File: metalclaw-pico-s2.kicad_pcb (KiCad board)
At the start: 2 copper layers, 21 x 51 mm, 73 parts, among them J1 USB_C_Receptacle_USB2.0_14P, J2 Conn_01x05, J3 Conn_02x05_Odd_Even, J4 Conn_Coaxial, SW1 SW_Push, SW2 SW_Push, U1 ESP32-S2, U2 MX25L3236FM2I-08G-TR, U3 APS6404L-3SQRx-SN, U5 XC6220B331MR, Y1 XRCGB40M000F1S2FR0

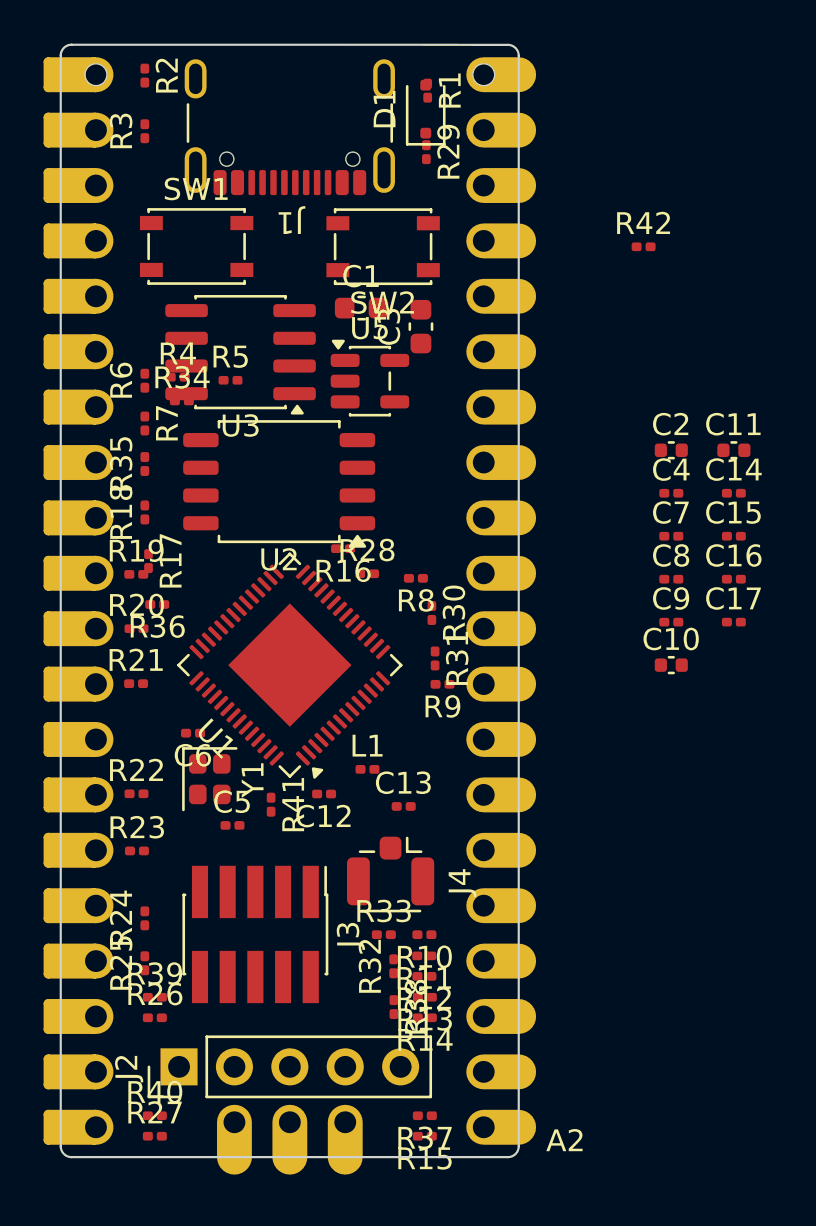
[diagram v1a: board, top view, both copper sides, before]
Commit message: Specify more passive component parts
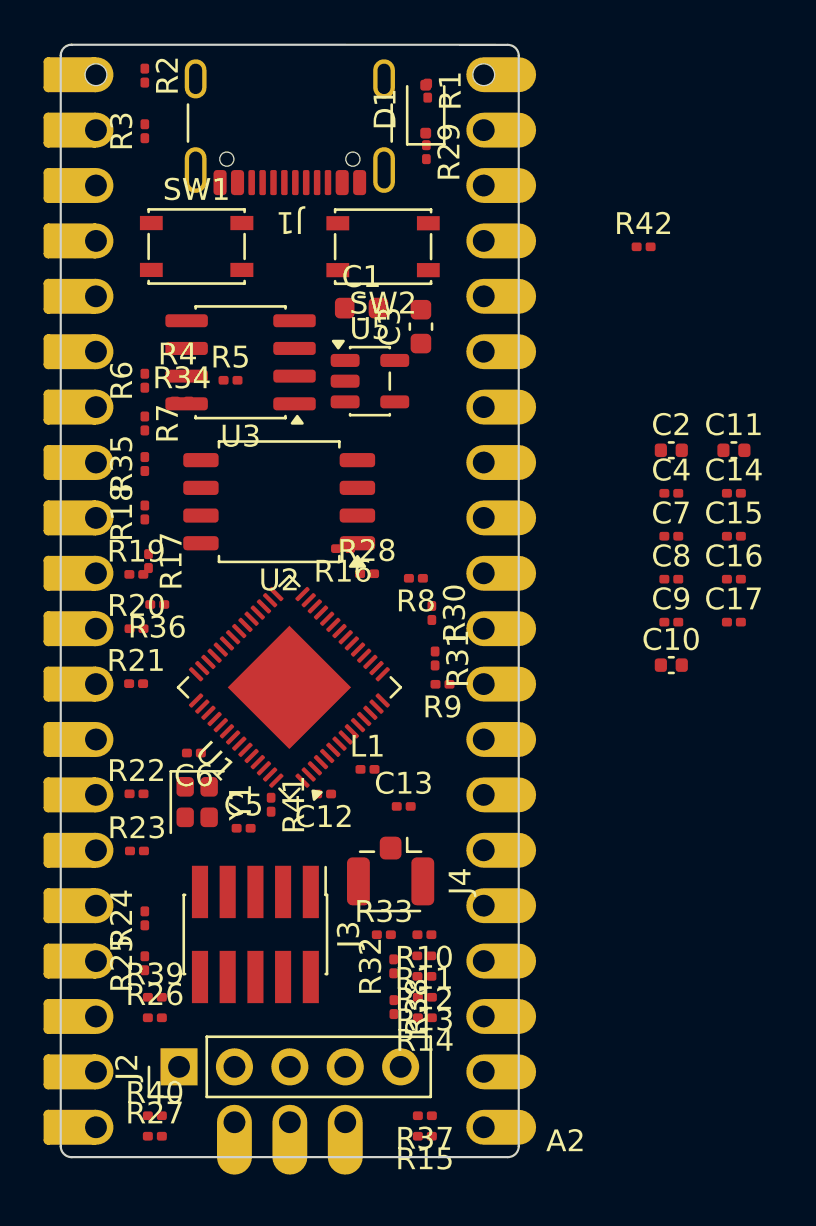
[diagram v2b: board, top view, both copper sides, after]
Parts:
- moved Y1 1.20 mm to (159.6, 108.1)
- moved U1 1.02 mm to (163.8, 102.8)
- moved U2 0.92 mm to (163.3, 94.3)
- moved C6 0.91 mm to (159.4, 105.8)
- moved C5 0.53 mm to (161.7, 109.3)
- moved U3 0.47 mm to (161.6, 87.9)
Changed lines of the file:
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@@
 	(footprint "Capacitor_SMD:C_0201_0603Metric"
 		(layer "F.Cu")
-		(at 161.18 109.16)
+		(at 161.69 109.29)
 		(descr "Capacitor SMD 0201 (0603 Metric), square (rectangular) end terminal, IPC-7351 nominal, (Body size source: https://www.vishay.com/docs/20052/crcw0201e3.pdf), generated with kicad-footprint-generator")
 		(tags "capacitor")
@@
 			)
 		)
-		(property "Mouser" "81-GJM0335C1H6R0CB1D"
+		(property "Mouser" "81-GRM0335C1E6R0BA1D "
 			(at 0 0 0)
 			(unlocked yes)
@@
 			)
 		)
+		(property "Mouser" "81-GRM033R61A104ME5D "
+			(at 0 0 0)
+			(unlocked yes)
+			(layer "F.Fab")
+			(hide yes)
+			(effects
+				(font
+					(size 1 1)
+					(thickness 0.15)
+				)
+			)
+		)
 		(property ki_fp_filters "C_*")
 		(sheetname "/")
@@
 			)
 		)
+		(property "Mouser" "81-GRM033R61A104ME5D "
+			(at 0 0 0)
+			(unlocked yes)
+			(layer "F.Fab")
+			(hide yes)
+			(effects
+				(font
+					(size 1 1)
+					(thickness 0.15)
+				)
+			)
+		)
 		(property ki_fp_filters "C_*")
 		(sheetname "/")
@@
 			)
 		)
+		(property "Mouser" "81-GRM033R61A104ME5D "
+			(at 0 0 0)
+			(unlocked yes)
+			(layer "F.Fab")
+			(hide yes)
+			(effects
+				(font
+					(size 1 1)
+					(thickness 0.15)
+				)
+			)
+		)
 		(property ki_fp_filters "C_*")
 		(sheetname "/")
@@
 			)
 		)
+		(property "Mouser" "81-GRM033R61A104ME5D "
+			(at 0 0 0)
+			(unlocked yes)
+			(layer "F.Fab")
+			(hide yes)
+			(effects
+				(font
+					(size 1 1)
+					(thickness 0.15)
+				)
+			)
+		)
 		(property ki_fp_filters "C_*")
 		(sheetname "/")
@@
 	(footprint "Package_SO:SOIC-8_5.3x5.3mm_P1.27mm"
 		(layer "F.Cu")
-		(at 163.32 93.3975 180)
+		(at 163.32 94.3175 180)
 		(descr "SOIC, 8 Pin (JEITA/EIAJ ED-7311-19 variation 08-001-BBA and Atmel/Microchip, 208 mils width, https://www.jeita.or.jp/japanese/standard/book/ED-7311-19/#target/page_no=21, https://ww1.microchip.com/downloads/en/DeviceDoc/20005045C.pdf#page=23, https://ww1.microchip.com/downloads/en/DeviceDoc/doc2535.pdf#page=162), generated with kicad-footprint-generator ipc_gullwing_generator.py")
 		(tags "SOIC SO P-SOP SOP SOP-8 SO SO-8 8S2 S2AE/F K04-056 CASE-751BE SO8W 8-Pin-SOIC PSA W8-2 W8-4 W8MS-1 FPT-8P-M08")
@@
 	(footprint "Crystal:Crystal_SMD_2016-4Pin_2.0x1.6mm"
 		(layer "F.Cu")
-		(at 160.14 107.04 -90)
+		(at 159.56 108.09 -90)
 		(descr "SMD2016/4, Crystal, 2.0x1.6mm package, SMD, generated with kicad-footprint-generator make_crystal.py, http://www.q-crystal.com/upload/5/2015552223166229.pdf")
 		(property "Reference" "Y1"
@@
 			)
 		)
-		(property "Mouser" "0603X106M100CT"
+		(property "Mouser" "791-0603X106M100CT "
 			(at 0 0 0)
 			(unlocked yes)
@@
 			)
 		)
+		(property "Mouser" "791-0201X105M100CT "
+			(at 0 0 0)
+			(unlocked yes)
+			(layer "F.Fab")
+			(hide yes)
+			(effects
+				(font
+					(size 1 1)
+					(thickness 0.15)
+				)
+			)
+		)
 		(property ki_fp_filters "C_*")
 		(sheetname "/")
@@
 			)
 		)
-		(property "Mouser" "0603X106M100CT"
+		(property "Mouser" "791-0603X106M100CT "
 			(at 0 0 90)
 			(unlocked yes)
@@
 			)
 		)
+		(property "Mouser" "81-GRM033R61A104ME5D "
+			(at 0 0 0)
+			(unlocked yes)
+			(layer "F.Fab")
+			(hide yes)
+			(effects
+				(font
+					(size 1 1)
+					(thickness 0.15)
+				)
+			)
+		)
 		(property ki_fp_filters "C_*")
 		(sheetname "/")
@@
 			)
 		)
+		(property "Mouser" "81-GRM033R61A104ME5D "
+			(at 0 0 0)
+			(unlocked yes)
+			(layer "F.Fab")
+			(hide yes)
+			(effects
+				(font
+					(size 1 1)
+					(thickness 0.15)
+				)
+			)
+		)
 		(property ki_fp_filters "C_*")
 		(sheetname "/")
@@
 			)
 		)
+		(property "Mouser" "81-GRM033R61A104ME5D "
+			(at 0 0 0)
+			(unlocked yes)
+			(layer "F.Fab")
+			(hide yes)
+			(effects
+				(font
+					(size 1 1)
+					(thickness 0.15)
+				)
+			)
+		)
 		(property ki_fp_filters "C_*")
 		(sheetname "/")
@@
 			)
 		)
+		(property "Mouser" "791-0201X105M100CT "
+			(at 0 0 0)
+			(unlocked yes)
+			(layer "F.Fab")
+			(hide yes)
+			(effects
+				(font
+					(size 1 1)
+					(thickness 0.15)
+				)
+			)
+		)
 		(property ki_fp_filters "C_*")
 		(sheetname "/")
@@
 			)
 		)
+		(property "Mouser" "81-GRM033R61A104ME5D "
+			(at 0 0 0)
+			(unlocked yes)
+			(layer "F.Fab")
+			(hide yes)
+			(effects
+				(font
+					(size 1 1)
+					(thickness 0.15)
+				)
+			)
+		)
 		(property ki_fp_filters "C_*")
 		(sheetname "/")
@@
 			)
 		)
+		(property "Mouser" "791-0201X105M100CT "
+			(at 0 0 0)
+			(unlocked yes)
+			(layer "F.Fab")
+			(hide yes)
+			(effects
+				(font
+					(size 1 1)
+					(thickness 0.15)
+				)
+			)
+		)
 		(property ki_fp_filters "C_*")
 		(sheetname "/")
@@
 	(footprint "Capacitor_SMD:C_0201_0603Metric"
 		(layer "F.Cu")
-		(at 159.37 104.93 180)
+		(at 159.41 105.84 180)
 		(descr "Capacitor SMD 0201 (0603 Metric), square (rectangular) end terminal, IPC-7351 nominal, (Body size source: https://www.vishay.com/docs/20052/crcw0201e3.pdf), generated with kicad-footprint-generator")
 		(tags "capacitor")
@@
 			)
 		)
-		(property "Mouser" "81-GJM0335C1H6R0CB1D "
+		(property "Mouser" "81-GRM0335C1E6R0BA1D "
 			(at 0 0 180)
 			(unlocked yes)
@@
 	(footprint "Package_SO:SOIC-8_3.9x4.9mm_P1.27mm"
 		(layer "F.Cu")
-		(at 161.55 87.46 180)
+		(at 161.55 87.925 180)
 		(descr "SOIC, 8 Pin (JEDEC MS-012AA, https://www.analog.com/media/en/package-pcb-resources/package/pkg_pdf/soic_narrow-r/r_8.pdf), generated with kicad-footprint-generator ipc_gullwing_generator.py")
 		(tags "SOIC SO")
@@
 	)
 	(footprint "Package_DFN_QFN:QFN-56-1EP_7x7mm_P0.4mm_EP4x4mm"
-		(locked yes)
 		(layer "F.Cu")
-		(at 163.81 101.812004 135)
+		(at 163.789548 102.829548 135)
 		(descr "QFN, 56 Pin (https://www.espressif.com/sites/default/files/documentation/esp32-s2_datasheet_en.pdf#page=41), generated with kicad-footprint-generator ipc_noLead_generator.py")
 		(tags "QFN NoLead")

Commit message: Some refinements to schematic and layout
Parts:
- C16, C17: value 100n -> 1u
- moved C17 27.4 mm to (163.8, 81.5)
- moved C15 26.0 mm to (160.4, 106.4), turned to 180 degrees
- moved C16 25.0 mm to (163.8, 83.4)
- moved C9 23.3 mm to (158.4, 104.4), turned to 180 degrees
- moved C14 21.3 mm to (167.1, 106.8)
- moved C11 20.1 mm to (169.1, 105.1)
- moved C8 20.0 mm to (161.3, 98.2), turned to 180 degrees
- moved R42 16.2 mm to (163.8, 82.5)
- moved C7 15.6 mm to (165.8, 97.9)
- moved C4 14.6 mm to (168.0, 100.1)
- moved C10 12.5 mm to (169.6, 106.3)
- moved C2 12.1 mm to (169.6, 94.8)
- moved L1 2.69 mm to (166.3, 109.0)
- moved C12 0.65 mm to (166.0, 107.7)
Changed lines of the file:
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@@
 	(footprint "Capacitor_SMD:C_0201_0603Metric"
 		(layer "F.Cu")
-		(at 181.3 95.9)
+		(at 165.85 97.89)
 		(descr "Capacitor SMD 0201 (0603 Metric), square (rectangular) end terminal, IPC-7351 nominal, (Body size source: https://www.vishay.com/docs/20052/crcw0201e3.pdf), generated with kicad-footprint-generator")
 		(tags "capacitor")
@@
 	(footprint "Capacitor_SMD:C_0201_0603Metric"
 		(layer "F.Cu")
-		(at 181.3 99.84)
+		(at 158.43 104.44 180)
 		(descr "Capacitor SMD 0201 (0603 Metric), square (rectangular) end terminal, IPC-7351 nominal, (Body size source: https://www.vishay.com/docs/20052/crcw0201e3.pdf), generated with kicad-footprint-generator")
 		(tags "capacitor")
@@
 		)
 		(property "Mouser" "81-GRM033R61A104ME5D "
-			(at 0 0 0)
+			(at 0 0 180)
 			(unlocked yes)
 			(layer "F.Fab")
@@
 		)
 		(pad "" smd roundrect
-			(at -0.345 0)
+			(at -0.345 0 180)
 			(size 0.318 0.36)
 			(layers "F.Paste")
@@
 		)
 		(pad "" smd roundrect
-			(at 0.345 0)
+			(at 0.345 0 180)
 			(size 0.318 0.36)
 			(layers "F.Paste")
@@
 		)
 		(pad "1" smd roundrect
-			(at -0.32 0)
+			(at -0.32 0 180)
 			(size 0.46 0.4)
 			(layers "F.Cu" "F.Mask")
@@
 		)
 		(pad "2" smd roundrect
-			(at 0.32 0)
+			(at 0.32 0 180)
 			(size 0.46 0.4)
 			(layers "F.Cu" "F.Mask")
@@
 	(footprint "Capacitor_SMD:C_0201_0603Metric"
 		(layer "F.Cu")
-		(at 181.3 93.93)
+		(at 168.02 100.07)
 		(descr "Capacitor SMD 0201 (0603 Metric), square (rectangular) end terminal, IPC-7351 nominal, (Body size source: https://www.vishay.com/docs/20052/crcw0201e3.pdf), generated with kicad-footprint-generator")
 		(tags "capacitor")
@@
 	(footprint "Capacitor_SMD:C_0201_0603Metric"
 		(layer "F.Cu")
-		(at 184.17 95.9)
+		(at 160.395 106.39 180)
 		(descr "Capacitor SMD 0201 (0603 Metric), square (rectangular) end terminal, IPC-7351 nominal, (Body size source: https://www.vishay.com/docs/20052/crcw0201e3.pdf), generated with kicad-footprint-generator")
 		(tags "capacitor")
@@
 		)
 		(property "Mouser" "81-GRM033R61A104ME5D "
-			(at 0 0 0)
+			(at 0 0 180)
 			(unlocked yes)
 			(layer "F.Fab")
@@
 		)
 		(pad "" smd roundrect
-			(at -0.345 0)
+			(at -0.345 0 180)
 			(size 0.318 0.36)
 			(layers "F.Paste")
@@
 		)
 		(pad "" smd roundrect
-			(at 0.345 0)
+			(at 0.345 0 180)
 			(size 0.318 0.36)
 			(layers "F.Paste")
@@
 		)
 		(pad "1" smd roundrect
-			(at -0.32 0)
+			(at -0.32 0 180)
 			(size 0.46 0.4)
 			(layers "F.Cu" "F.Mask")
@@
 		)
 		(pad "2" smd roundrect
-			(at 0.32 0)
+			(at 0.32 0 180)
 			(size 0.46 0.4)
 			(layers "F.Cu" "F.Mask")
@@
 	(footprint "Inductor_SMD:L_0201_0603Metric"
 		(layer "F.Cu")
-		(at 167.37 106.59)
+		(at 166.275 109.05)
 		(descr "Inductor SMD 0201 (0603 Metric), square (rectangular) end terminal, IPC-7351 nominal, (Body size source: https://www.vishay.com/docs/20052/crcw0201e3.pdf), generated with kicad-footprint-generator")
 		(tags "inductor")
@@
 		(sheetname "/")
 		(sheetfile "metalclaw-pico-s2.kicad_sch")
-		(attr smd)
+		(attr smd dnp)
 		(fp_rect
 			(start -0.7 -0.35)
@@
 	(footprint "Capacitor_SMD:C_0402_1005Metric"
 		(layer "F.Cu")
-		(at 184.17 91.96)
+		(at 169.06 105.14)
 		(descr "Capacitor SMD 0402 (1005 Metric), square (rectangular) end terminal, IPC-7351 nominal, (Body size source: IPC-SM-782 page 76, https://www.pcb-3d.com/wordpress/wp-content/uploads/ipc-sm-782a_amendment_1_and_2.pdf), generated with kicad-footprint-generator")
 		(tags "capacitor")
@@
 	(footprint "Capacitor_SMD:C_0201_0603Metric"
 		(layer "F.Cu")
-		(at 184.17 99.84)
+		(at 163.825 81.5)
 		(descr "Capacitor SMD 0201 (0603 Metric), square (rectangular) end terminal, IPC-7351 nominal, (Body size source: https://www.vishay.com/docs/20052/crcw0201e3.pdf), generated with kicad-footprint-generator")
 		(tags "capacitor")
@@
 			)
 		)
-		(property "Value" "100n"
+		(property "Value" "1u"
 			(at 0 1.05 0)
 			(layer "F.Fab")
@@
 	(footprint "Capacitor_SMD:C_0201_0603Metric"
 		(layer "F.Cu")
-		(at 184.17 93.93)
+		(at 167.145 106.78)
 		(descr "Capacitor SMD 0201 (0603 Metric), square (rectangular) end terminal, IPC-7351 nominal, (Body size source: https://www.vishay.com/docs/20052/crcw0201e3.pdf), generated with kicad-footprint-generator")
 		(tags "capacitor")
@@
 	(footprint "Capacitor_SMD:C_0201_0603Metric"
 		(layer "F.Cu")
-		(at 181.3 97.87)
+		(at 161.32 98.17 180)
 		(descr "Capacitor SMD 0201 (0603 Metric), square (rectangular) end terminal, IPC-7351 nominal, (Body size source: https://www.vishay.com/docs/20052/crcw0201e3.pdf), generated with kicad-footprint-generator")
 		(tags "capacitor")
@@
 		)
 		(property "Mouser" "81-GRM033R61A104ME5D "
-			(at 0 0 0)
+			(at 0 0 180)
 			(unlocked yes)
 			(layer "F.Fab")
@@
 		)
 		(pad "" smd roundrect
-			(at -0.345 0)
+			(at -0.345 0 180)
 			(size 0.318 0.36)
 			(layers "F.Paste")
@@
 		)
 		(pad "" smd roundrect
-			(at 0.345 0)
+			(at 0.345 0 180)
 			(size 0.318 0.36)
 			(layers "F.Paste")
@@
 		)
 		(pad "1" smd roundrect
-			(at -0.32 0)
+			(at -0.32 0 180)
 			(size 0.46 0.4)
 			(layers "F.Cu" "F.Mask")
@@
 		)
 		(pad "2" smd roundrect
-			(at 0.32 0)
+			(at 0.32 0 180)
 			(size 0.46 0.4)
 			(layers "F.Cu" "F.Mask")
@@
 	(footprint "Capacitor_SMD:C_0402_1005Metric"
 		(layer "F.Cu")
-		(at 181.3 91.96)
+		(at 169.55 94.81)
 		(descr "Capacitor SMD 0402 (1005 Metric), square (rectangular) end terminal, IPC-7351 nominal, (Body size source: IPC-SM-782 page 76, https://www.pcb-3d.com/wordpress/wp-content/uploads/ipc-sm-782a_amendment_1_and_2.pdf), generated with kicad-footprint-generator")
 		(tags "capacitor")
@@
 		(sheetname "/")
 		(sheetfile "metalclaw-pico-s2.kicad_sch")
-		(attr smd)
+		(attr smd dnp)
 		(fp_rect
 			(start -0.7 -0.35)
@@
 	(footprint "Capacitor_SMD:C_0201_0603Metric"
 		(layer "F.Cu")
-		(at 184.17 97.87)
+		(at 163.805 83.36)
 		(descr "Capacitor SMD 0201 (0603 Metric), square (rectangular) end terminal, IPC-7351 nominal, (Body size source: https://www.vishay.com/docs/20052/crcw0201e3.pdf), generated with kicad-footprint-generator")
 		(tags "capacitor")
@@
 			)
 		)
-		(property "Value" "100n"
+		(property "Value" "1u"
 			(at 0 1.05 0)
 			(layer "F.Fab")
@@
 	(footprint "Resistor_SMD:R_0201_0603Metric"
 		(layer "F.Cu")
-		(at 180.03 82.63)
+		(at 163.81 82.52)
 		(descr "Resistor SMD 0201 (0603 Metric), square (rectangular) end terminal, IPC-7351 nominal, (Body size source: https://www.vishay.com/docs/20052/crcw0201e3.pdf), generated with kicad-footprint-generator")
 		(tags "resistor")
@@
 	(footprint "Capacitor_SMD:C_0402_1005Metric"
 		(layer "F.Cu")
-		(at 181.3 101.81)
+		(at 169.62 106.3)
 		(descr "Capacitor SMD 0402 (1005 Metric), square (rectangular) end terminal, IPC-7351 nominal, (Body size source: IPC-SM-782 page 76, https://www.pcb-3d.com/wordpress/wp-content/uploads/ipc-sm-782a_amendment_1_and_2.pdf), generated with kicad-footprint-generator")
 		(tags "capacitor")
@@
 	)
 	(footprint "Package_DFN_QFN:QFN-56-1EP_7x7mm_P0.4mm_EP4x4mm"
+		(locked yes)
 		(layer "F.Cu")
 		(at 163.789548 102.829548 135)
@@
 		(sheetname "/")
 		(sheetfile "metalclaw-pico-s2.kicad_sch")
-		(attr smd)
+		(attr smd dnp)
 		(fp_rect
 			(start -0.515 -0.94)
@@
 	(footprint "Capacitor_SMD:C_0201_0603Metric"
 		(layer "F.Cu")
-		(at 165.38 107.72 180)
+		(at 166.025 107.74 180)
 		(descr "Capacitor SMD 0201 (0603 Metric), square (rectangular) end terminal, IPC-7351 nominal, (Body size source: https://www.vishay.com/docs/20052/crcw0201e3.pdf), generated with kicad-footprint-generator")
 		(tags "capacitor")
@@
 		(sheetname "/")
 		(sheetfile "metalclaw-pico-s2.kicad_sch")
-		(attr smd)
+		(attr smd dnp)
 		(fp_rect
 			(start -0.7 -0.35)

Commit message: Fix all ERC errors and warnings
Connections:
- A2 pad 33: GND -> Net-(A2-AGND)
- R17 pad 2: /GP6 -> /GP7
- R19 pad 2: /GP6 -> /GP7
- R27 pad 2: /GP14 -> /GP15
- R31 pad 2: /GP14 -> /GP15
- R40 pad 2: /GP14 -> /GP15
- U1 pad 21: /GP6 -> /GP7
- U1 pad 30: +3V3 -> VDD
- U1 pad 55: /GP14 -> /GP15
- U2 pad 8: +3.3V -> VDD
- U3 pad 8: +3.3V -> VDD
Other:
- copper layers 2 -> 4
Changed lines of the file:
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@@
 	(layers
 		(0 "F.Cu" signal)
+		(4 "In1.Cu" signal)
+		(6 "In2.Cu" signal)
 		(2 "B.Cu" signal)
 		(9 "F.Adhes" user "F.Adhesive")
@@
 	)
 	(setup
+		(stackup
+			(layer "F.SilkS"
+				(type "Top Silk Screen")
+			)
+			(layer "F.Paste"
+				(type "Top Solder Paste")
+			)
+			(layer "F.Mask"
+				(type "Top Solder Mask")
+				(thickness 0.01)
+			)
+			(layer "F.Cu"
+				(type "copper")
+				(thickness 0.035)
+			)
+			(layer "dielectric 1"
+				(type "prepreg")
+				(thickness 0.1)
+				(material "FR4")
+				(epsilon_r 4.5)
+				(loss_tangent 0.02)
+			)
+			(layer "In1.Cu"
+				(type "copper")
+				(thickness 0.035)
+			)
+			(layer "dielectric 2"
+				(type "core")
+				(thickness 1.24)
+				(material "FR4")
+				(epsilon_r 4.5)
+				(loss_tangent 0.02)
+			)
+			(layer "In2.Cu"
+				(type "copper")
+				(thickness 0.035)
+			)
+			(layer "dielectric 3"
+				(type "prepreg")
+				(thickness 0.1)
+				(material "FR4")
+				(epsilon_r 4.5)
+				(loss_tangent 0.02)
+			)
+			(layer "B.Cu"
+				(type "copper")
+				(thickness 0.035)
+			)
+			(layer "B.Mask"
+				(type "Bottom Solder Mask")
+				(thickness 0.01)
+			)
+			(layer "B.Paste"
+				(type "Bottom Solder Paste")
+			)
+			(layer "B.SilkS"
+				(type "Bottom Silk Screen")
+			)
+			(copper_finish "None")
+			(dielectric_constraints no)
+		)
 		(pad_to_mask_clearance 0)
 		(allow_soldermask_bridges_in_footprints no)
@@
 	(net 74 "/GP14")
 	(net 75 "/MTDI")
-	(net 76 "+3.3V")
+	(net 76 "Net-(A2-AGND)")
 	(net 77 "+3V3")
 	(net 78 "Net-(J1-CC2)")
@@
 	(net 86 "Net-(J4-In)")
 	(net 87 "Net-(U1-LNA_IN)")
+	(net 88 "/GP7")
+	(net 89 "/GP15")
+	(net 90 "VDD")
 	(footprint "Resistor_SMD:R_0201_0603Metric"
 		(layer "F.Cu")
@@
 			(layers "F.Cu" "F.Mask")
 			(roundrect_rratio 0.25)
-			(net 74 "/GP14")
+			(net 89 "/GP15")
 			(pintype "passive")
 		)
@@
 			(remove_unused_layers no)
 			(roundrect_rratio 0.5)
-			(net 4 "GND")
+			(net 76 "Net-(A2-AGND)")
 			(pinfunction "AGND")
 			(pintype "power_out")
@@
 			(layers "F.Cu" "F.Mask")
 			(roundrect_rratio 0.25)
-			(net 48 "/GP6")
+			(net 88 "/GP7")
 			(pintype "passive")
 		)
@@
 			(layers "F.Cu" "F.Mask")
 			(roundrect_rratio 0.25)
-			(net 74 "/GP14")
+			(net 89 "/GP15")
 			(pintype "passive")
 		)
@@
 			(layers "F.Cu" "F.Mask" "F.Paste")
 			(roundrect_rratio 0.25)
-			(net 76 "+3.3V")
+			(net 90 "VDD")
 			(pinfunction "VCC")
 			(pintype "power_in")
@@
 		)
 		(fp_text user "${REFERENCE}"
-			(at 23.619096 8.5 90)
+			(at 0 0 90)
 			(layer "F.Fab")
 			(effects
@@
 			)
 		)
-		(property "Mouser" "81-GRM033R61A104ME5D "
+		(property "Mouser" "791-0201X105M100CT "
 			(at 0 0 0)
 			(unlocked yes)
@@
 			(layers "F.Cu" "F.Mask")
 			(roundrect_rratio 0.25)
-			(net 48 "/GP6")
+			(net 88 "/GP7")
 			(pintype "passive")
 		)
@@
 			)
 		)
-		(property "Mouser" "81-GRM033R61A104ME5D "
+		(property "Mouser" "791-0201X105M100CT "
 			(at 0 0 0)
 			(unlocked yes)
@@
 			(layers "F.Cu" "F.Mask")
 			(roundrect_rratio 0.25)
-			(net 74 "/GP14")
+			(net 89 "/GP15")
 			(pintype "passive")
 		)
@@
 			(layers "F.Cu" "F.Mask" "F.Paste")
 			(roundrect_rratio 0.25)
-			(net 76 "+3.3V")
+			(net 90 "VDD")
 			(pinfunction "VDD")
 			(pintype "power_in")
@@
 			(layers "F.Cu" "F.Mask" "F.Paste")
 			(roundrect_rratio 0.25)
-			(net 48 "/GP6")
+			(net 88 "/GP7")
 			(pinfunction "XTAL_32K_P")
 			(pintype "passive")
@@
 			(layers "F.Cu" "F.Mask" "F.Paste")
 			(roundrect_rratio 0.25)
-			(net 77 "+3V3")
+			(net 90 "VDD")
 			(pinfunction "VDD_SPI")
 			(pintype "power_out")
@@
 			(layers "F.Cu" "F.Mask" "F.Paste")
 			(roundrect_rratio 0.25)
-			(net 74 "/GP14")
+			(net 89 "/GP15")
 			(pinfunction "GPIO46")
 			(pintype "input")
